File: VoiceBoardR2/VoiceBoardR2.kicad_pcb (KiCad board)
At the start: 4 copper layers, 130 x 50 mm, 157 parts, among them J101 VoiceHeader, Q201 BC857, Q202 BC857, Q301 BC858, Q302 BC858, Q401 BC858, Q402 BC857, Q403 BC847, Q404 BC857, Q405 BC847, Q406 BC858, U101 TMUX4053, U102 TMUX4053, U201 TL074, U202 TL074, U203 MCP4451-104E-ST, U204 TL074, U205 MCP4451-104E-ST, U206 TL072, U301 TL074, U303 LM13700, U304 MCP4018-103E/LT, U402 LM13700, U403 TL074, U404 TL074

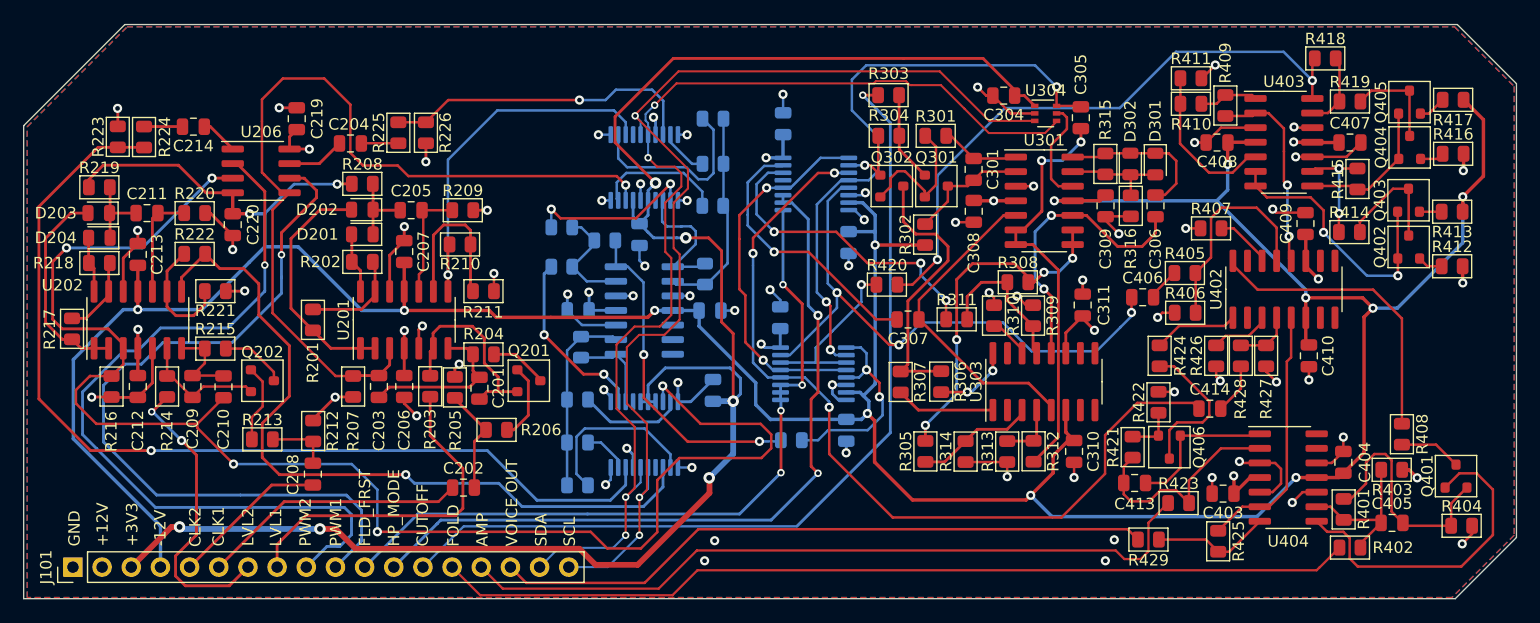
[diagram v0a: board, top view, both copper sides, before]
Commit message: new saw to tri converter
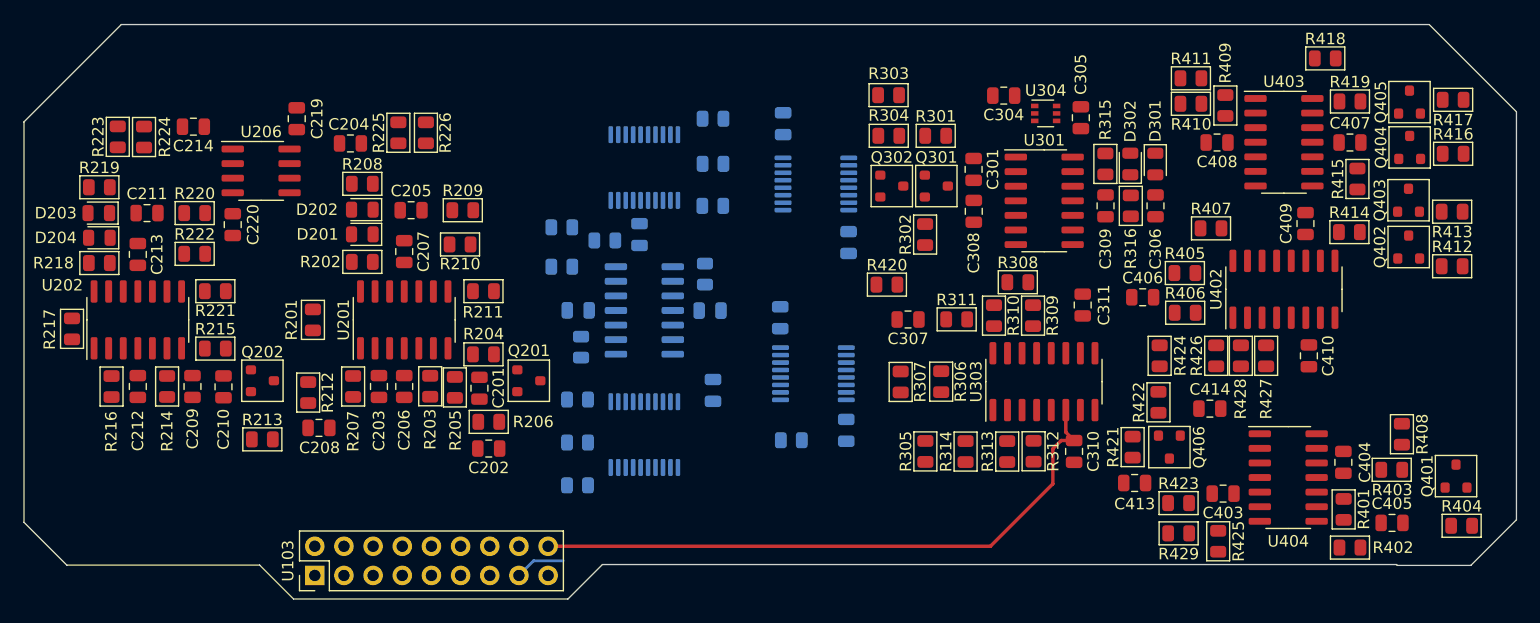
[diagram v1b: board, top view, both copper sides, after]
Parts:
- removed J101: VoiceHeader, Connector_PinHeader_2.54mm:PinHeader_1x18_P2.54mm_Vertical
- added U103: VoiceBoardConn_18P_254P, Connector_PinHeader_2.54mm:PinHeader_2x09_P2.54mm_Vertical, F.Cu at (25.4, 48.0)
- moved C208 4.06 mm to (25.7, 35.1), turned to 180 degrees
- moved C202 4.05 mm to (40.5, 36.9), turned to 180 degrees
- moved R212 3.38 mm to (24.8, 32.0)
- moved R429 2.68 mm to (100.6, 44.3)
- moved R206 0.97 mm to (40.5, 34.6)
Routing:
- net -12V: track 319.7 -> 54.4 mm, vias 14 -> 0
- net GND: track 161.4 -> 0.00 mm, vias 67 -> 0
- net +3.3V: track 156.4 -> 4.37 mm, vias 6 -> 0
- net SAW2_FULL: track 130.2 -> 0.00 mm, vias 5 -> 0
- net SDA: track 95.1 -> 0.00 mm, vias 4 -> 0
- net SCL: track 93.7 -> 0.00 mm, vias 3 -> 0
- net PULSE2_FULL: track 84.9 -> 0.00 mm, vias 1 -> 0
- net FOLD_CV: track 80.0 -> 0.00 mm
- net CUTOFF_CV: track 77.3 -> 0.00 mm, vias 1 -> 0
- net SAW1_FULL: track 75.0 -> 0.00 mm, vias 1 -> 0
- net VCA_IN: track 74.9 -> 0.00 mm, vias 3 -> 0
- net PWM_2_CV: track 68.9 -> 0.00 mm, vias 1 -> 0
- net PWM_1_CV: track 67.6 -> 0.00 mm, vias 1 -> 0
- net HP_MODE: track 66.8 -> 0.00 mm, vias 2 -> 0
- net TRI2_FULL: track 66.2 -> 0.00 mm, vias 1 -> 0
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- removed copper zone on B.Cu, net GND
- removed copper zone on F.Cu, net GND
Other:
- outline, holes or cut-outs redrawn
- board text removed: "+12V"
- board text removed: "+3V3"
- board text removed: "-12V"
- board text removed: "AMP"
- board text removed: "CLK1"
- board text removed: "CLK2"
- board text removed: "CUTOFF"
- board text removed: "FLD_FRST"
- board text removed: "FOLD"
- board text removed: "GND"
- board text removed: "HP_MODE"
- board text removed: "LVL1"
- board text removed: "LVL2"
- board text removed: "PWM1"
- board text removed: "PWM2"
- board text removed: "SCL"
- board text removed: "SDA"
- board text removed: "VOICE OUT"

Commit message: op-amp layout improved
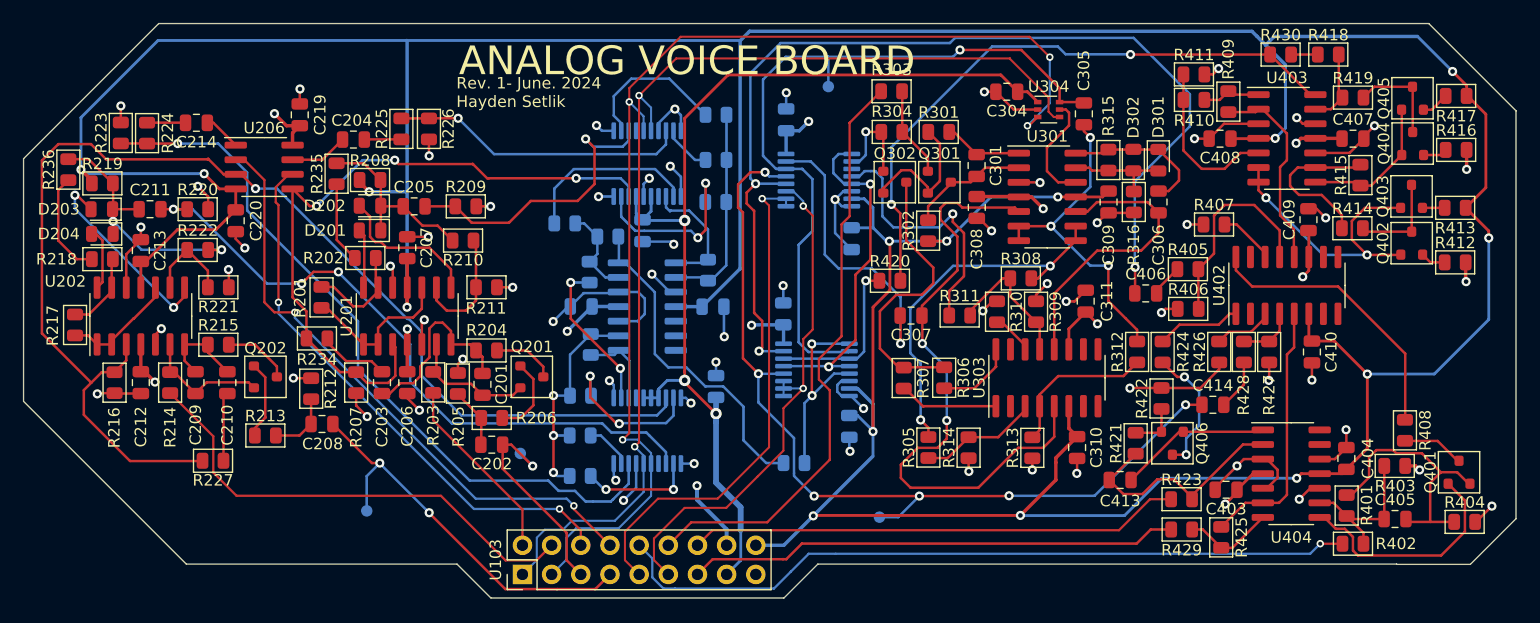
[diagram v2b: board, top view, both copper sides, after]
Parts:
- added R227: 68k, PCM_Resistor_SMD_AKL:R_0805_2012Metric, F.Cu at (16.5, 38.0)
- added R234: 68k, PCM_Resistor_SMD_AKL:R_0805_2012Metric, F.Cu at (25.5, 27.3)
- added R235: 10k, PCM_Resistor_SMD_AKL:R_0805_2012Metric, F.Cu at (27.2, 13.0)
- added R236: 10k, PCM_Resistor_SMD_AKL:R_0805_2012Metric, F.Cu at (3.89, 12.6)
- added R430: 33k, PCM_Resistor_SMD_AKL:R_0805_2012Metric, F.Cu at (109.5, 2.61)
- added TP101: FLTR_OUT, TestPoint:TestPoint_Pad_D1.0mm_Value, B.Cu at (70.1, 5.40)
- added TP102: VCA_IN, TestPoint:TestPoint_Pad_D1.0mm_Value, B.Cu at (74.5, 42.9)
- added TP103: CLK_2, TestPoint:TestPoint_Pad_D1.0mm_Value, B.Cu at (29.9, 42.4)
- added TP104: CLK_1, TestPoint:TestPoint_Pad_D1.0mm_Value, B.Cu at (43.2, 37.4)
- R204, R215: value 1k -> 470
- R207, R216, R418: value 220k -> 100k
- R223, R226: value 100k -> 39k
- R224, R225: value 220k -> 92k
- R309, R310, R313, R314: value 220 -> 470
- R410: value 100k -> 47k
- R425: value 22k -> 33k
- moved U103 18.1 mm to (43.4, 47.9)
- moved R312 12.5 mm to (97.0, 28.5), turned to 90 degrees
- moved R240 2.47 mm to (49.3, 21.6), turned to 90 degrees
- moved R313 2.21 mm to (87.8, 36.9)
- moved R201 2.10 mm to (25.9, 23.8)
- moved R242 2.00 mm to (67.1, 38.2)
- moved C413 1.29 mm to (95.5, 39.7)
- moved R232 0.88 mm to (49.4, 27.9)
- moved R237 0.85 mm to (48.5, 39.3)
- moved D202 0.75 mm to (30.2, 15.8)
- moved D201 0.75 mm to (30.2, 17.9)
- moved R208 0.75 mm to (30.2, 13.5)
- moved R238 0.66 mm to (48.5, 35.8)
- moved C210 0.50 mm to (17.7, 31.2)
- moved C103 0.43 mm to (71.9, 35.0)
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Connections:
- C203 pad 2: SAW1_FULL -> Net-(C203-Pad2)
- C205 pad 2: Net-(U201C-+) -> TRI1_FULL
- C210 pad 2: SAW2_FULL -> Net-(C210-Pad2)
- C211 pad 2: Net-(U202C-+) -> TRI2_FULL
- R201 pad 1: Net-(D202-A) -> Net-(U201A--)
- R202 pad 2: Net-(D201-A) -> Net-(R202-Pad2)
- R209 pad 1: Net-(U201C-+) -> TRI1_FULL
- R210 pad 2: TRI1_FULL -> Net-(D201-K)
- R217 pad 1: Net-(D203-A) -> Net-(U202A--)
- R218 pad 2: Net-(D204-A) -> Net-(R218-Pad2)
- R220 pad 1: Net-(U202C-+) -> TRI2_FULL
- R222 pad 2: TRI2_FULL -> Net-(D203-K)
- R420 pad 2: Net-(R418-Pad1) -> Net-(R420-Pad2)
- U102 pad 11: HP_MODE -> FOLD_FIRST
- U102 pad 12: FILTER_IN -> FOLDER_IN
- U102 pad 13: unconnected-(U102-A1-Pad13) -> VCA_IN
- U102 pad 14: LP_IN -> FILTER_OUT
- U102 pad 3: VCA_IN -> unconnected-(U102-C1-Pad3)
- U102 pad 4: FILTER_OUT -> LP_IN
- U102 pad 5: FOLDER_IN -> FILTER_IN
- U102 pad 9: FOLD_FIRST -> HP_MODE
- U201 pad 1: Net-(D202-A) -> Net-(U201A--)
- U201 pad 10: Net-(U201C-+) -> Net-(U201A--)
- U201 pad 2: Net-(D202-A) -> Net-(U201A--)
- U201 pad 8: TRI1_FULL -> Net-(D202-A)
- U202 pad 1: Net-(D203-A) -> Net-(U202A--)
- U202 pad 10: Net-(U202C-+) -> Net-(U202A--)
- U202 pad 2: Net-(D203-A) -> Net-(U202A--)
- U202 pad 8: TRI2_FULL -> Net-(D203-A)
- U403 pad 14: Net-(R418-Pad1) -> Net-(R420-Pad2)
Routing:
- net -12V: track 54.4 -> 416.4 mm, vias 0 -> 15
- net GND: track 0.00 -> 185.0 mm, vias 0 -> 64
- net SAW2_FULL: track 0.00 -> 109.5 mm, vias 0 -> 1
- net SCL: track 0.00 -> 100.4 mm, vias 0 -> 4
- net SDA: track 0.00 -> 94.0 mm, vias 0 -> 2
- net FOLDER_IN: track 0.00 -> 91.1 mm, vias 0 -> 3
- net +3.3V: track 4.37 -> 89.9 mm, vias 0 -> 3
- net VCA_IN: track 0.00 -> 78.1 mm, vias 0 -> 6
- net FILTER_OUT: track 0.00 -> 65.6 mm, vias 0 -> 1
- net FOLD_CV: track 0.00 -> 65.4 mm, vias 0 -> 1
- net PULSE2_FULL: track 0.00 -> 63.9 mm, vias 0 -> 1
- net SAW1_FULL: track 0.00 -> 59.3 mm, vias 0 -> 3
- net TRI2_FULL: track 0.00 -> 57.7 mm, vias 0 -> 3
- net +12V: track 0.00 -> 55.7 mm, vias 0 -> 14
- net Net-(U301B-+): track 0.00 -> 54.5 mm, vias 0 -> 2
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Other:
- outline, holes or cut-outs redrawn
- board text added: "ANALOG VOICE BOARD"
- board text added: "Rev. 1- June. 2024 Hayden Setlik"
